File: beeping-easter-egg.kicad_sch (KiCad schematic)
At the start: 14 parts, among them Q1 AO3401A, Q2 AO3401A, SW1 YUEN FUNG ST-0-102-A01-T000-LF, U1 TLC555CDR

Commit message: Set title
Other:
- company: (none) -> github.com/DougTomanio/beeping-easter-egg
- title: github.com/DougTomanio/beeping-easter-egg -> Beeping Easter Egg
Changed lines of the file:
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@@
 	(paper "A5")
 	(title_block
-		(title "github.com/DougTomanio/beeping-easter-egg")
+		(title "Beeping Easter Egg")
 		(rev "A")
+		(company "github.com/DougTomanio/beeping-easter-egg")
 	)
 	(rectangle

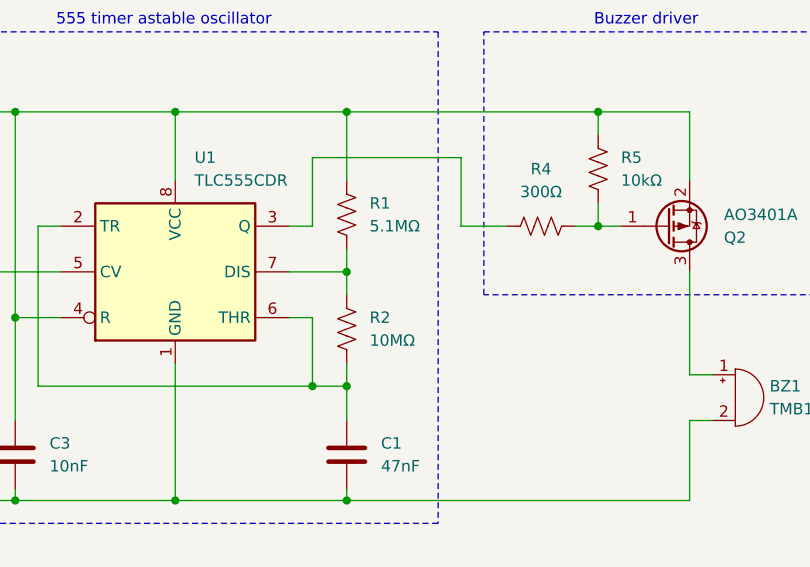
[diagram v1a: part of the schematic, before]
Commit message: Update component values to reflect corrected timing calculations
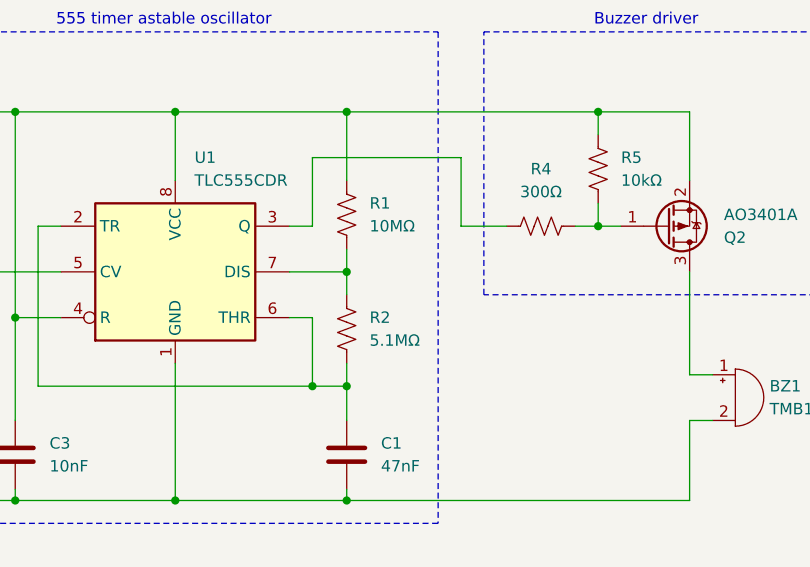
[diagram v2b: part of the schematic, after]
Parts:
- R1: value 5.1MΩ -> 10MΩ; LCSC C13320 -> C7250
- R2: value 10MΩ -> 5.1MΩ; LCSC C7250 -> C13320
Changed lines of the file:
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@@
 			)
 		)
-		(property "Value" "5.1MΩ"
+		(property "Value" "10MΩ"
 			(at 143.51 57.1499 0)
 			(effects
@@
 			)
 		)
-		(property "LCSC" "C13320"
+		(property "LCSC" "C7250"
 			(at 140.97 55.88 0)
 			(effects
@@
 			)
 		)
-		(property "Value" "10MΩ"
+		(property "Value" "5.1MΩ"
 			(at 143.51 69.8499 0)
 			(effects
@@
 			)
 		)
-		(property "LCSC" "C7250"
+		(property "LCSC" "C13320"
 			(at 140.97 68.58 0)
 			(effects

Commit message: Update title
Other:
- company: github.com/DougTomanio/beeping-easter-egg -> (none)
- title: Beeping Easter Egg -> github.com/DougTomanio/beeping-easter-egg
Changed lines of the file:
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@@
 	(paper "A5")
 	(title_block
-		(title "Beeping Easter Egg")
+		(title "github.com/DougTomanio/beeping-easter-egg")
 		(rev "B")
-		(company "github.com/DougTomanio/beeping-easter-egg")
 	)
 	(rectangle
